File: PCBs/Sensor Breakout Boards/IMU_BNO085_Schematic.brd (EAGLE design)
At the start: 25.4 x 25.4 mm, 8 parts, among them J1 2X6 FEMALE

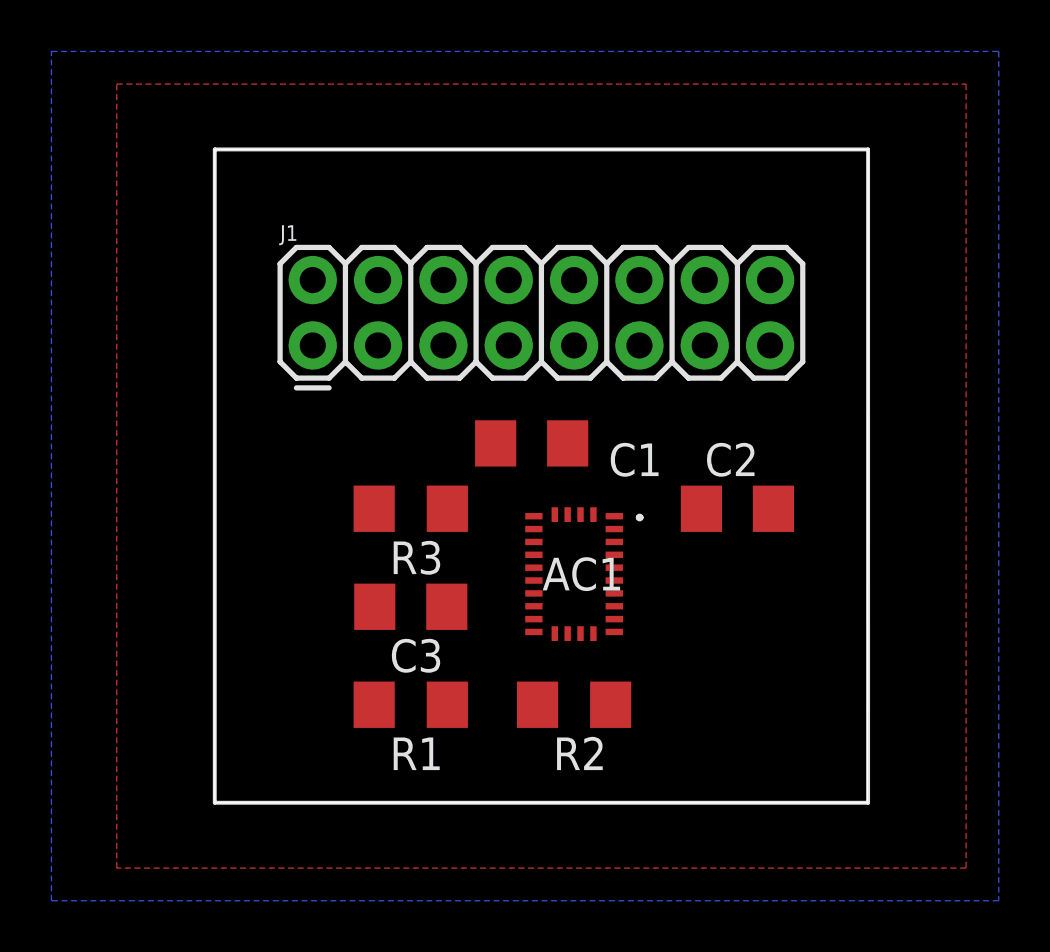
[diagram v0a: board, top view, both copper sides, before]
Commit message: Laid out board + redid library for BNO
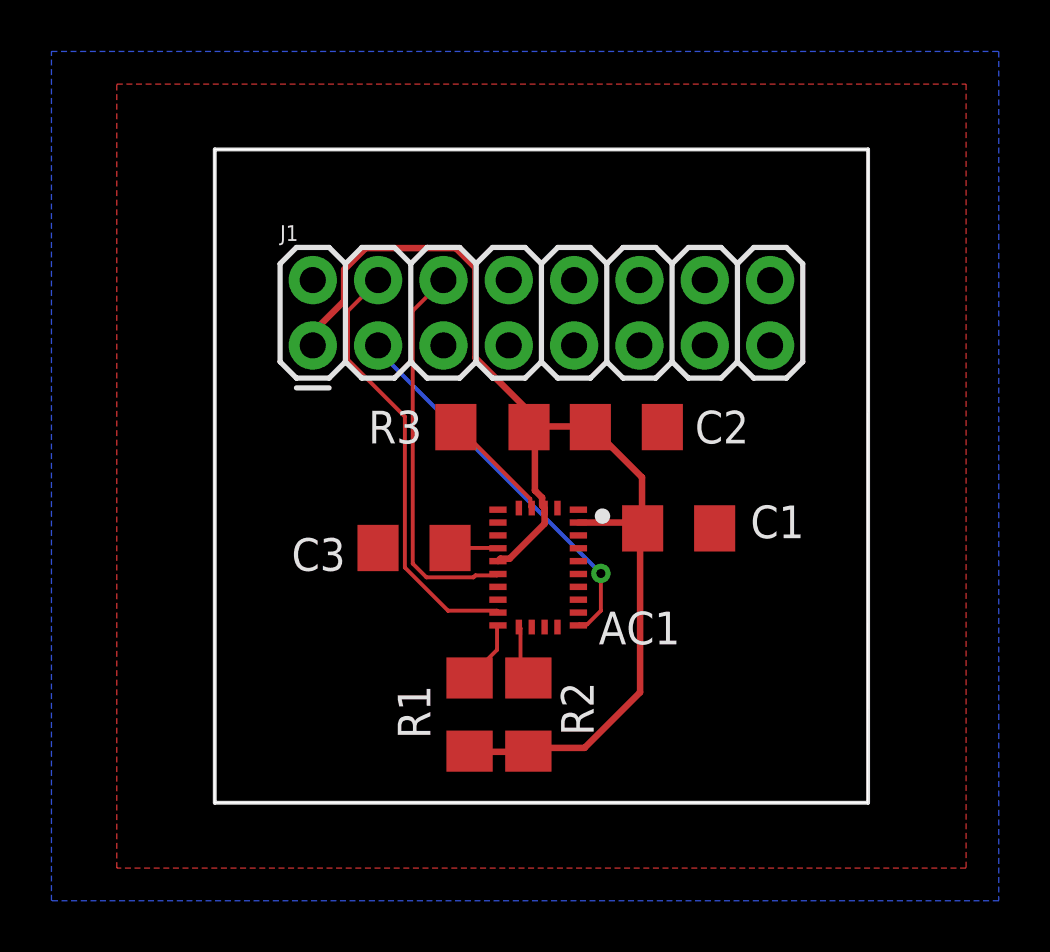
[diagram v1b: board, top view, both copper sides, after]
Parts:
- R1, R2: value (none) -> 2.2k
- R3: value (none) -> 10k
- moved C1 6.60 mm to (18.0, 10.7), turned to 0 degrees
- moved C2 5.36 mm to (16.0, 14.6)
- moved R3 4.49 mm to (10.8, 14.6), turned to 0 degrees
- moved R1 2.32 mm to (9.91, 3.43), turned to 270 degrees
- moved C3 2.29 mm to (7.75, 9.91)
- moved R2 1.82 mm to (12.2, 3.43), turned to 270 degrees
- moved AC1 1.42 mm to (12.6, 9.14)
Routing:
- net VCC: track 0.00 -> 46.5 mm
- net INT: track 0.00 -> 16.9 mm
- net RST: track 0.00 -> 15.1 mm
- net SDA: track 0.00 -> 15.0 mm, vias 0 -> 1
- net N$8: track 0.00 -> 4.45 mm
- net N$2: track 0.00 -> 2.50 mm
- net N$1: track 0.00 -> 2.14 mm
- net N$3: track 0.00 -> 1.86 mm

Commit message: some cleanup
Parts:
- moved C2 1.52 mm to (16.0, 13.1)
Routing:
- net VCC: track 46.5 -> 41.3 mm
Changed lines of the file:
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@@
 <setting verticaltext="up"/>
 </settings>
-<grid distance="5" unitdist="mil" unit="mil" style="lines" multiple="1" display="no" altdistance="5" altunitdist="mil" altunit="mil"/>
+<grid distance="20" unitdist="mil" unit="mil" style="lines" multiple="1" display="no" altdistance="5" altunitdist="mil" altunit="mil"/>
 <layers>
 <layer number="1" name="Top" color="4" fill="1" visible="yes" active="yes"/>
@@
 <attribute name="MOUSER_PRICE-STOCK" value="" x="12.573" y="9.144" size="1.778" layer="27" display="off"/>
 <attribute name="NAME" x="16.51" y="6.794" size="1.27" layer="25" align="center"/>
-<attribute name="VALUE" x="12.573" y="5.144" size="1.27" layer="27" align="center"/>
+<attribute name="VALUE" x="11.176" y="7.176" size="1.27" layer="27" align="center"/>
 </element>
 <element name="C1" library="RTR Main Library" package="C1206" value="0.1u" x="18.034" y="10.668" smashed="yes">
@@
 <attribute name="VALUE" x="20.828" y="8.509" size="1.27" layer="27"/>
 </element>
-<element name="C2" library="RTR Main Library" package="C1206" value="0.1u" x="16.002" y="14.605" smashed="yes">
-<attribute name="NAME" x="18.669" y="13.97" size="1.27" layer="25"/>
-<attribute name="VALUE" x="18.669" y="12.319" size="1.27" layer="27"/>
+<element name="C2" library="RTR Main Library" package="C1206" value="0.1u" x="16.002" y="13.081" smashed="yes">
+<attribute name="NAME" x="18.669" y="12.446" size="1.27" layer="25"/>
+<attribute name="VALUE" x="15.113" y="14.351" size="1.27" layer="27"/>
 </element>
 </elements>
@@
 <contactref element="C2" pad="2"/>
 <contactref element="C1" pad="2"/>
+<wire x1="11.823" y1="11.457" x2="13.323" y2="11.457" width="0" layer="19" extent="1-1"/>
+<wire x1="11.01" y1="11.394" x2="11.823" y2="11.457" width="0" layer="19" extent="1-1"/>
 </signal>
 <signal name="VCC" class="2">
@@
 <wire x1="12.192" y1="1.9812" x2="12.192" y2="2.007" width="0.254" layer="1"/>
 <wire x1="12.2682" y1="14.6304" x2="12.446" y2="14.6304" width="0.254" layer="1"/>
-<wire x1="12.446" y1="14.6304" x2="14.5542" y2="14.6304" width="0.254" layer="1"/>
-<wire x1="14.5542" y1="14.6304" x2="14.602" y2="14.605" width="0.254" layer="1"/>
+<wire x1="14.5542" y1="13.1064" x2="14.602" y2="13.081" width="0.254" layer="1"/>
 <wire x1="12.2682" y1="14.6304" x2="12.217" y2="14.605" width="0.254" layer="1"/>
-<wire x1="16.6116" y1="12.6492" x2="16.6116" y2="10.668" width="0.254" layer="1"/>
-<wire x1="14.7066" y1="14.5542" x2="16.6116" y2="12.6492" width="0.254" layer="1"/>
 <wire x1="16.6116" y1="10.668" x2="16.634" y2="10.668" width="0.254" layer="1"/>
-<wire x1="14.7066" y1="14.5542" x2="14.602" y2="14.605" width="0.254" layer="1"/>
 <wire x1="16.5354" y1="4.2926" x2="14.3764" y2="2.1336" width="0.254" layer="1"/>
 <wire x1="12.192" y1="2.1336" x2="14.3764" y2="2.1336" width="0.254" layer="1"/>
@@
 <wire x1="12.192" y1="14.7066" x2="12.217" y2="14.605" width="0.254" layer="1"/>
 <wire x1="3.81" y1="17.8308" x2="3.81" y2="17.78" width="0.254" layer="1"/>
-<wire x1="12.823" y1="11.457" x2="12.7274" y2="11.5526" width="0.254" layer="1"/>
-<wire x1="12.7274" y1="11.5526" x2="12.7274" y2="11.86023125" width="0.254" layer="1"/>
-<wire x1="12.446" y1="12.14163125" x2="12.446" y2="14.6304" width="0.254" layer="1"/>
-<wire x1="12.7274" y1="11.86023125" x2="12.446" y2="12.14163125" width="0.254" layer="1"/>
 <wire x1="14.136" y1="10.894" x2="16.2332" y2="10.894" width="0.254" layer="1"/>
 <wire x1="16.2332" y1="10.894" x2="16.5354" y2="10.5918" width="0.254" layer="1"/>
@@
 <wire x1="12.823" y1="11.457" x2="12.823" y2="10.84936875" width="0.254" layer="1"/>
 <wire x1="12.823" y1="10.84936875" x2="11.46323125" y2="9.4896" width="0.254" layer="1"/>
+<wire x1="12.823" y1="11.457" x2="12.823" y2="12.569" width="0.254" layer="1"/>
+<wire x1="13.3604" y1="13.1064" x2="14.5542" y2="13.1064" width="0.254" layer="1"/>
+<wire x1="12.823" y1="12.569" x2="13.3604" y2="13.1064" width="0.254" layer="1"/>
+<wire x1="12.217" y1="14.605" x2="13.3604" y2="13.4616" width="0.254" layer="1"/>
+<wire x1="13.3604" y1="13.4616" x2="13.3604" y2="13.1064" width="0.254" layer="1"/>
+<wire x1="14.136" y1="10.894" x2="12.823" y2="11.457" width="0" layer="19" extent="1-1"/>
 </signal>
 <signal name="SCL">
 <contactref element="J1" pad="5"/>
 <contactref element="AC1" pad="19"/>
+<wire x1="13.323" y1="6.831" x2="8.89" y2="17.78" width="0" layer="19" extent="1-1"/>
 </signal>
 <signal name="SDA">
@@
 <wire x1="9.4488" y1="14.6304" x2="9.373" y2="14.605" width="0.1524" layer="1"/>
 </signal>
+<signal name="N$4">
+<via x="10.16" y="12.192" extent="1-16" drill="0.35"/>
+</signal>
 </signals>

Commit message: Prep for JLC?
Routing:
- net SCL: track 0.00 -> 16.9 mm, vias 0 -> 1
- net VCC: track 41.3 -> 45.8 mm
- net GND: track 0.00 -> 0.84 mm, vias 0 -> 1
- net N$8: track 4.45 -> 5.05 mm
